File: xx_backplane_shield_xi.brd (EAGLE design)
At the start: 65.7 x 97.8 mm, 31 parts, among them U7 LM2678

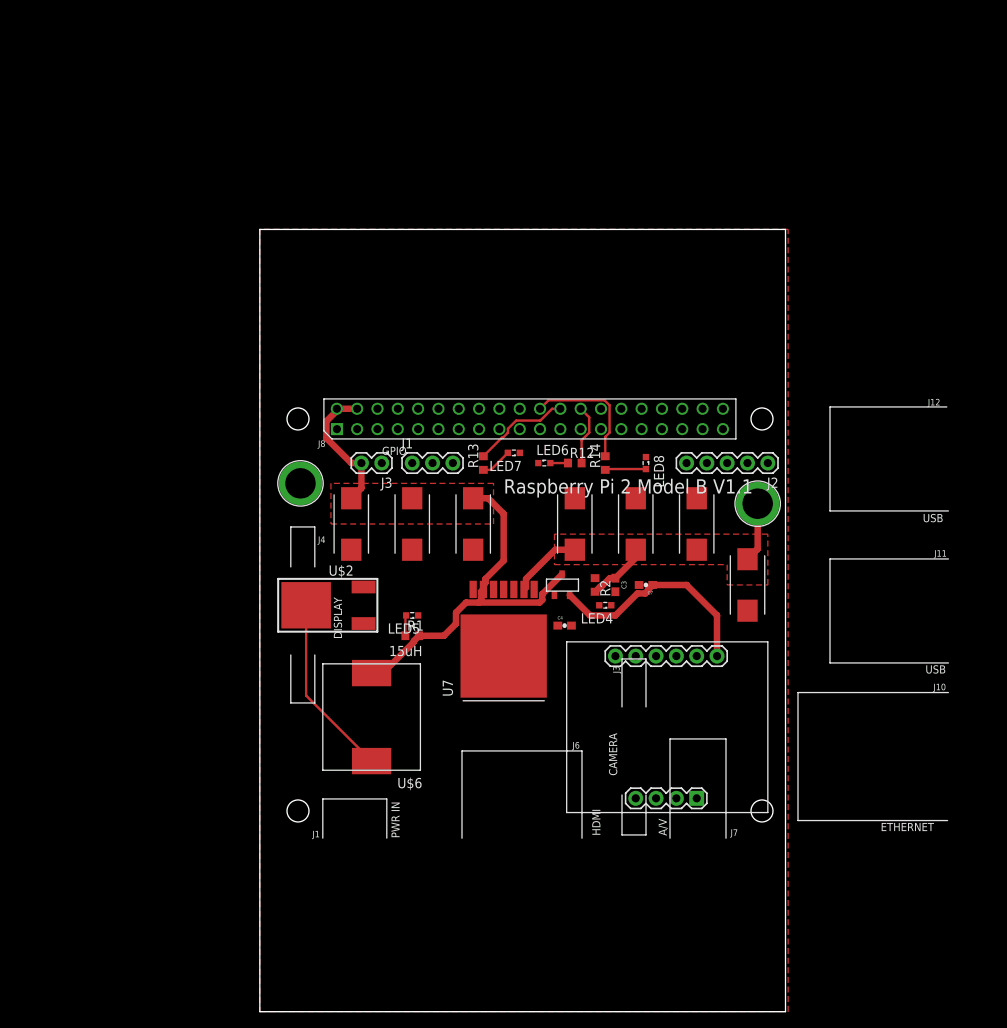
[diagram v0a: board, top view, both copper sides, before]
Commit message: Cleaning up eagle file and renaming board name
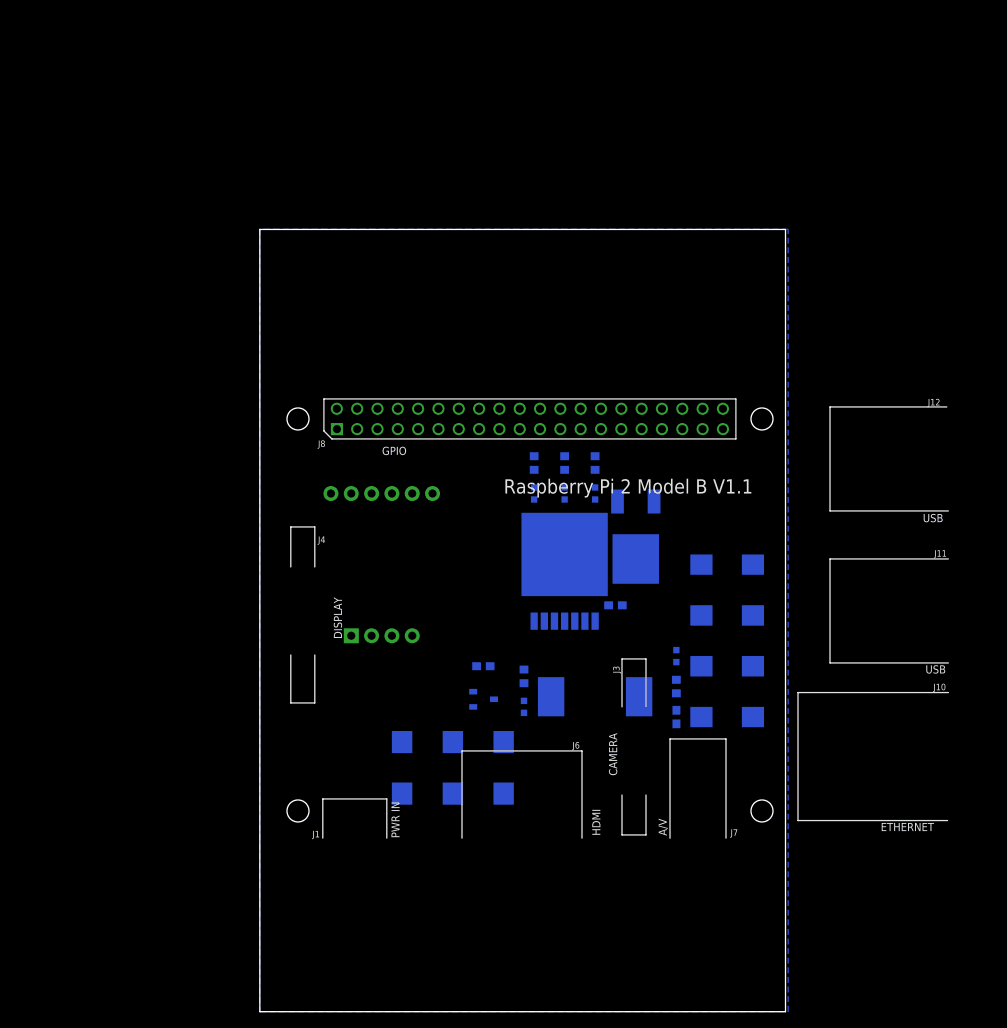
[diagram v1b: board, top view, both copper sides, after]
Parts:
- removed J1: (no value), SparkFun-Connectors:1X03
- removed J2: (no value), SparkFun-Connectors:1X05
- removed J3: (no value), SparkFun-Connectors:1X02
- removed V+_ESC1, V+_ESC5: (no value), SparkFun-Connectors:BANANA_CONN
- moved U$3 43.2 mm to (14.0, 40.6), flipped to the bottom
- moved U$2 39.1 mm to (47.0, 44.5), flipped to the bottom, turned to 90 degrees
- moved C6 32.6 mm to (30.5, 15.2), flipped to the bottom
- moved C10 31.1 mm to (17.8, 15.2), flipped to the bottom
- moved C13 30.7 mm to (58.4, 21.6), flipped to the bottom, turned to 180 degrees
- moved C9 30.6 mm to (24.1, 15.2), flipped to the bottom
- moved U$6 28.1 mm to (41.9, 24.1), flipped to the bottom, turned to 90 degrees
- moved C7 22.7 mm to (27.9, 27.9), flipped to the bottom
- moved C3 18.2 mm to (52.1, 21.6), flipped to the bottom
- moved LED5 18.1 mm to (33.0, 22.9), flipped to the bottom, turned to 90 degrees
- moved U$5 17.3 mm to (26.7, 22.9), flipped to the bottom, turned to 90 degrees
- moved R2 16.3 mm to (52.1, 25.4), flipped to the bottom
- moved R1 14.9 mm to (33.0, 26.7), flipped to the bottom, turned to 90 degrees
- moved U7 14.8 mm to (38.1, 41.9), flipped to the bottom, turned to 270 degrees
- moved LED8 14.5 mm to (34.3, 49.5), flipped to the bottom, turned to 90 degrees
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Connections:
- removed net RX_BT: J2.3
- removed net TX_BT: J2.2
- net +12V: no longer V+_ESC5.P$1
- net +5V: no longer J3.2
- net GND: no longer J1.1, J2.1, J3.1, V+_ESC1.P$1
- net MISO: no longer J2.5
- net MOSI: no longer J2.4
- net SCL: no longer J1.2
- net SDA: no longer J1.3
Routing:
- net +5V: track 64.6 -> 0.00 mm
- net 3.3V: track 27.8 -> 0.00 mm
- net +12V: track 24.3 -> 0.00 mm
- net N$19: track 22.9 -> 0.00 mm
- net LED3: track 16.0 -> 0.00 mm
- net LED2: track 12.4 -> 0.00 mm
- net LED1: track 7.62 -> 0.00 mm
- net N$15: track 5.12 -> 0.00 mm
- net N$14: track 3.94 -> 0.00 mm
- net N$2: track 2.58 -> 0.00 mm
- net N$13: track 2.21 -> 0.00 mm
- added copper zone on layer 16, net GND
- removed copper zone on layer 1, net +12V
- removed copper zone on layer 1, net +5V
- removed copper zone on layer 1, net GND

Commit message: deleted like everything
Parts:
- removed C10, C6, C9: 150uF, PowerComponents:CTAN(7.30_4.30MM)
- removed C11, C12, C13, C2: 10uF, PowerComponents:CTAN(7.30_4.30MM)
- removed C3: 0.47uF, SparkFun-Capacitors:0603
- removed C4: 0.01uF, SparkFun-Passives:0603-CAP
- removed LED4: (no value), led:SML0603
- removed R2: 1k, resistor:R0603
- removed U$6: 15uH, DiscreteComponents:HCMA1305
- removed U7: LM2678, PowerComponents:LM2678
- added U$1: T2I, BackplaneParts:T2I
- U$2: value SWITCHMODE_SCHOTTKY -> T2I5P; device PowerComponents:DPAK-3 -> BackplaneParts:T2I5P
- moved LED5 43.1 mm to (2.54, 53.3)
- moved R1 36.8 mm to (7.62, 53.3), turned to 270 degrees
- moved U$5 32.1 mm to (8.89, 49.5), turned to 270 degrees
- moved C7 22.5 mm to (12.7, 44.5)
- moved U$2 21.3 mm to (40.6, 64.8), flipped to the top, turned to 0 degrees
- moved U$3 2.54 mm to (16.5, 40.6)
- moved LED6 2.54 mm to (39.4, 49.5)
- moved LED7 2.54 mm to (35.6, 49.5)
- moved LED8 2.54 mm to (31.8, 49.5)
- moved R12 2.54 mm to (39.4, 53.3)
- moved R13 2.54 mm to (35.6, 53.3)
- moved R14 2.54 mm to (31.8, 53.3)
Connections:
- removed net +12V: C11.+, C12.+, C13.+, C2.+, C3.1, R2.2, U7.2
- removed net N$18: C4.1, U7.3
- removed net N$19: C4.2, U$2.P$4, U$6.P$1, U7.1
- removed net N$3: LED4.A, R2.1
- net +5V: now also U$2.P$5, U$2.P$6; no longer C10.+, C6.+, C9.+, U$6.P$2, U7.6
- net GND: now also U$2.P$2; no longer C10.-, C11.-, C12.-, C13.-, C2.-, C3.2, C6.-, C9.-, LED4.C, U$2.P$1, U7.4, U7.TAB
- net SCL: now also U$1.1
- net SDA: now also U$1.2
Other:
- board size 65.7 x 97.8 mm -> 41.6 x 43.2 mm

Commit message: finished board version 1
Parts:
- removed U$1: T2I, BackplaneParts:T2I
- added R2, R3: 330, resistor:R0603
- added U$4, U$6: THROUGHOLE, throughhole:THROUGHHOLE
- U$2: value T2I5P -> T2I; device BackplaneParts:T2I5P -> BackplaneParts:T2I
- moved R12 47.3 mm to (51.3, 7.62), flipped to the top
- moved R13 47.3 mm to (47.5, 7.62), flipped to the top
- moved R14 47.2 mm to (43.6, 7.62), flipped to the top
- moved LED5 46.8 mm to (12.7, 7.62), flipped to the top
- moved LED6 46.6 mm to (51.3, 4.45), flipped to the top
- moved LED7 46.6 mm to (47.5, 4.45), flipped to the top
- moved LED8 46.6 mm to (43.6, 4.45), flipped to the top
- moved R1 41.7 mm to (12.7, 11.9), flipped to the top, turned to 90 degrees
- moved U$2 34.9 mm to (21.5, 35.6), turned to 90 degrees
- moved U$3 24.1 mm to (40.6, 40.6), turned to 180 degrees
- moved U$5 16.1 mm to (24.1, 44.5), flipped to the top, turned to 0 degrees
- moved C7 12.8 mm to (25.3, 41.9), flipped to the top
- moved PCB1 4.75 mm to (2.54, 10.9), flipped to the bottom, turned to 90 degrees
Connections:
- removed net FIN: PCB1.P$33
- removed net LASER_ON: PCB1.P$29
- removed net MISO: PCB1.P$35
- removed net MOSI: PCB1.P$38
- removed net RX: PCB1.P$10
- removed net SCLK: PCB1.P$40
- removed net SERVO_PWM: PCB1.P$12
- removed net TX: PCB1.P$8
- net +5V: now also U$2.4, U$4.P$1; no longer U$2.P$5, U$2.P$6
- net 3.3V: now also R2.2, R3.2
- net GND: now also U$2.3, U$6.P$1; no longer U$2.P$2, U$2.P$3
- net LED1: now also PCB1.P$11; no longer PCB1.P$26
- net LED2: now also PCB1.P$13; no longer PCB1.P$24
- net LED3: now also PCB1.P$15; no longer PCB1.P$22
- net SCL: now also R3.1, U$2.2; no longer U$1.1
- net SDA: now also R2.1, U$2.1; no longer U$1.2
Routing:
- net +5V: track 0.00 -> 120.8 mm
- net SCL: track 0.00 -> 58.6 mm
- net SDA: track 0.00 -> 58.6 mm
- net LED3: track 0.00 -> 32.8 mm
- net RESET: track 0.00 -> 30.9 mm
- net LED2: track 0.00 -> 28.6 mm
- net LED1: track 0.00 -> 24.5 mm
- net 3.3V: track 0.00 -> 24.1 mm
- net N$2: track 0.00 -> 2.72 mm
- net N$15: track 0.00 -> 1.57 mm
- net N$14: track 0.00 -> 1.57 mm
- net N$13: track 0.00 -> 1.57 mm
- added copper zone on layer 1, net GND
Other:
- board size 41.6 x 43.2 mm -> 61 x 78.7 mm

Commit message: part placement almost done
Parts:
- removed LED6, LED7, LED8: (no value), led:SML0603
- removed R12, R13, R14: 330, resistor:R0603
- added C1, C3: 0.1u, SparkFun-Passives:0603-CAP
- added LED1, LED2, LED3, LED4: WS2812B5050, microbuilder:WS2812B
- added POWER: T2I5P, T2I5P:T2I5P
- added PS1, PS2: DF13-4P-1.25DSA, con-hirose-df13:DF13-4P-1.25DSA
- added R4, R6: 0 Ohms, resistor:R0603
- added R5, R7: 0 ohms, resistor:R0603
- moved U$2 72.8 mm to (71.0, 88.9), flipped to the bottom, turned to 270 degrees
- moved U$4 49.6 mm to (64.8, 15.2)
- moved R3 33.3 mm to (49.5, 26.2), flipped to the bottom, turned to 90 degrees
- moved U$5 29.6 mm to (44.5, 22.9), flipped to the bottom, turned to 270 degrees
- moved R2 29.2 mm to (49.1, 21.7), flipped to the bottom, turned to 270 degrees
- moved C7 21.0 mm to (45.7, 46.9), turned to 270 degrees
- moved LED5 18.5 mm to (30.5, 12.7), turned to 180 degrees
- moved R1 17.3 mm to (29.7, 15.2), turned to 0 degrees
- moved U$6 17.1 mm to (-3.81, 15.2)
- moved U$3 7.73 mm to (33.0, 41.9), turned to 0 degrees
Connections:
- removed net BT_LED_ON: PCB1.P$36
- removed net LED_ON: PCB1.P$31
- removed net N$13: LED6.A, R12.1
- removed net N$14: LED7.A, R13.1
- removed net N$15: LED8.A, R14.1
- new net N$1: PS1.P$2, R4.2
- new net N$10: PS2.P$3, R7.2
- new net N$11: POWER.P$5
- new net N$12: POWER.P$6
- new net N$3: LED1.2-DOUT, LED2.4-DIN
- new net N$4: LED2.2-DOUT, LED3.4-DIN
- new net N$5: LED3.2-DOUT, LED4.4-DIN
- new net N$8: PS1.P$3, R5.2
- new net N$9: PS2.P$2, R6.2
- new net NEO_PIXEL_IN: LED1.4-DIN, PCB1.P$12
- net +5V: now also C1.1, C3.1, LED1.1-VDD, LED2.1-VDD, LED3.1-VDD, LED4.1-VDD; no longer U$2.4
- net 3.3V: now also PS1.P$1, PS2.P$1
- net GND: now also C1.2, C3.2, LED1.3-GND, LED2.3-GND, LED3.3-GND, LED4.3-GND, POWER.P$2, POWER.P$3, PS1.P$4, PS2.P$4; no longer LED6.C, LED7.C, LED8.C, U$2.3
- net LED1: no longer R12.2
- net LED2: no longer R13.2
- net LED3: no longer R14.2
- net SCL: now also R4.1, R6.1
- net SDA: now also R5.1, R7.1, U$2.3; no longer U$2.1
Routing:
- net +5V: track 120.8 -> 0.00 mm
- net SCL: track 58.6 -> 0.00 mm
- net SDA: track 58.6 -> 0.00 mm
- net LED3: track 32.8 -> 0.00 mm
- net RESET: track 30.9 -> 0.00 mm
- net LED2: track 28.6 -> 0.00 mm
- net LED1: track 24.5 -> 0.00 mm
- net 3.3V: track 24.1 -> 0.00 mm
- net N$2: track 2.72 -> 0.00 mm
- net N$15: track 1.57 -> 0.00 mm
- net N$14: track 1.57 -> 0.00 mm
- net N$13: track 1.57 -> 0.00 mm
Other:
- board size 61 x 78.7 mm -> 80 x 82.5 mm

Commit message: half way done routing first revision
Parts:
- removed R6: 0 Ohms, resistor:R0603
- removed R7: 0 ohms, resistor:R0603
- added USB_CAM_POW: (no value), pinhead:1X03
- moved U$6 76.3 mm to (66.2, 45.5)
- moved U$4 75.4 mm to (-4.32, 45.5)
- moved PS2 21.0 mm to (68.1, 24.8)
- moved PS1 20.8 mm to (-6.50, 24.9)
- moved U$5 11.5 mm to (33.0, 22.4)
- moved C3 8.51 mm to (67.4, 52.5), turned to 180 degrees
- moved LED1 7.73 mm to (66.0, 33.0)
- moved U$3 7.62 mm to (31.4, 34.5)
- moved LED4 7.62 mm to (-3.81, 33.0)
- moved C1 6.29 mm to (-0.38, 51.9)
- moved R4 6.28 mm to (45.8, 24.4), flipped to the bottom, turned to 0 degrees
- moved R5 5.62 mm to (45.8, 21.9), flipped to the bottom, turned to 0 degrees
- moved LED2 1.80 mm to (66.0, 64.8)
- moved U$2 1.80 mm to (69.7, 87.6)
- moved POWER 1.80 mm to (-7.62, 68.6)
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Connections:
- removed net N$10: PS2.P$3, R7.2
- removed net N$11: POWER.P$5
- removed net N$12: POWER.P$6
- removed net N$9: PS2.P$2, R6.2
- net +5V: now also POWER.P$5, POWER.P$6, USB_CAM_POW.1
- net GND: now also USB_CAM_POW.3
- net SCL: now also PS2.P$2; no longer R6.1
- net SDA: now also PS2.P$3; no longer R7.1
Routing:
- net +5V: track 0.00 -> 119.1 mm
- net SDA: track 0.00 -> 94.3 mm
- net SCL: track 0.00 -> 86.1 mm
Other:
- outline, holes or cut-outs redrawn

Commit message: finished routing, need to add final touches
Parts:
- moved C3 18.5 mm to (66.4, 34.0)
- moved C7 11.9 mm to (37.0, 39.4), turned to 180 degrees
- moved C1 6.42 mm to (2.64, 46.3)
- moved R1 4.77 mm to (34.2, 13.7), turned to 90 degrees
- moved U$5 4.69 mm to (36.9, 19.8), flipped to the top, turned to 90 degrees
- moved U$6 0.44 mm to (65.8, 45.6)
- moved USB_CAM_POW 0.28 mm to (30.4, 72.1)
- moved LED5 0.06 mm to (30.4, 12.7), turned to 0 degrees
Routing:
- net +5V: track 119.1 -> 262.0 mm, vias 0 -> 5
- net 3.3V: track 0.00 -> 119.6 mm, vias 0 -> 3
- net N$4: track 0.00 -> 78.8 mm, vias 0 -> 2
- net N$8: track 0.00 -> 52.5 mm, vias 0 -> 1
- net N$1: track 0.00 -> 52.1 mm, vias 0 -> 1
- net N$5: track 0.00 -> 32.9 mm
- net N$3: track 0.00 -> 31.7 mm
- net NEO_PIXEL_IN: track 0.00 -> 10.7 mm, vias 0 -> 2
- net N$2: track 0.00 -> 3.12 mm
- net SDA: track 94.3 -> 93.6 mm

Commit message: made the fixes
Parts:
- added C2, C4: 0.1u, SparkFun-Passives:0603-CAP
- moved C1 19.8 mm to (-3.66, 65.1)
- moved LED5 2.37 mm to (28.5, 14.1)
- moved R1 1.20 mm to (34.3, 14.9)
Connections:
- net +5V: now also C2.1, C4.1
- net GND: now also C2.2, C4.2
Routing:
- net RESET: track 0.00 -> 24.3 mm
- net +5V: track 262.0 -> 267.9 mm, vias 5 -> 6
- net N$2: track 3.12 -> 5.10 mm
